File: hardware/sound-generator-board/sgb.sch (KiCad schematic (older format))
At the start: 53 parts, among them K1 CONN_3, P1 CONN_5, P10 CONN_4, P11 CONN_4, P12 CONN_4, P13 CONN_4, P14 CONN_4, P2 CONN_5, P4 CONN_6, P5 CONN_4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

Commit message: Turns out my transistor inverter isn't needed. That's good
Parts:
- removed P4: CONN_6, symbol CONN_6
- removed Q1: NPN, symbol NPN
- removed R4, R5: R, symbol R
- added K2: CONN_3, symbol CONN_3
- added unit 5 of U3
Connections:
- wire segments 340 -> 331

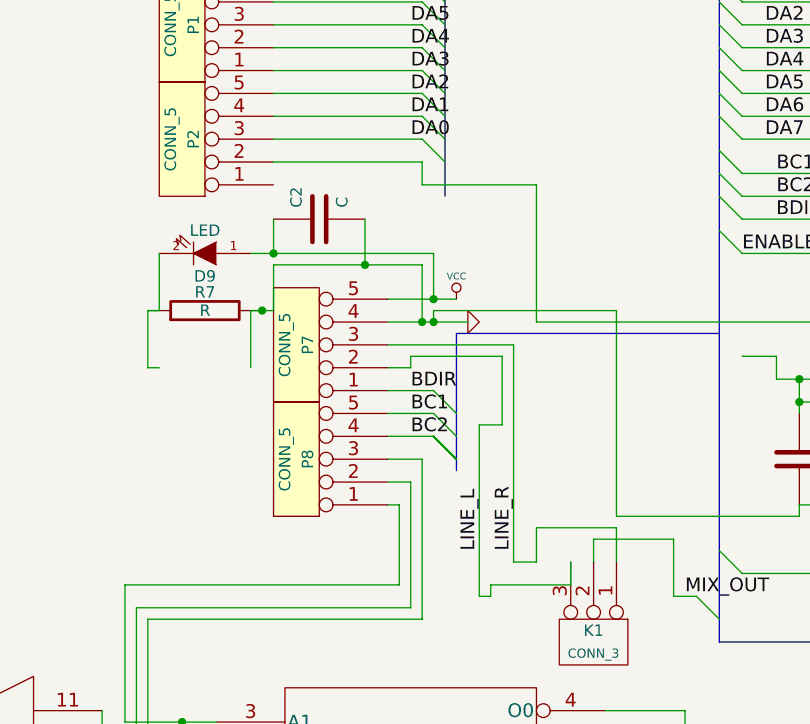
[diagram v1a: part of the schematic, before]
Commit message: Changed data bus pinout slightly to reduce noise on audio lines
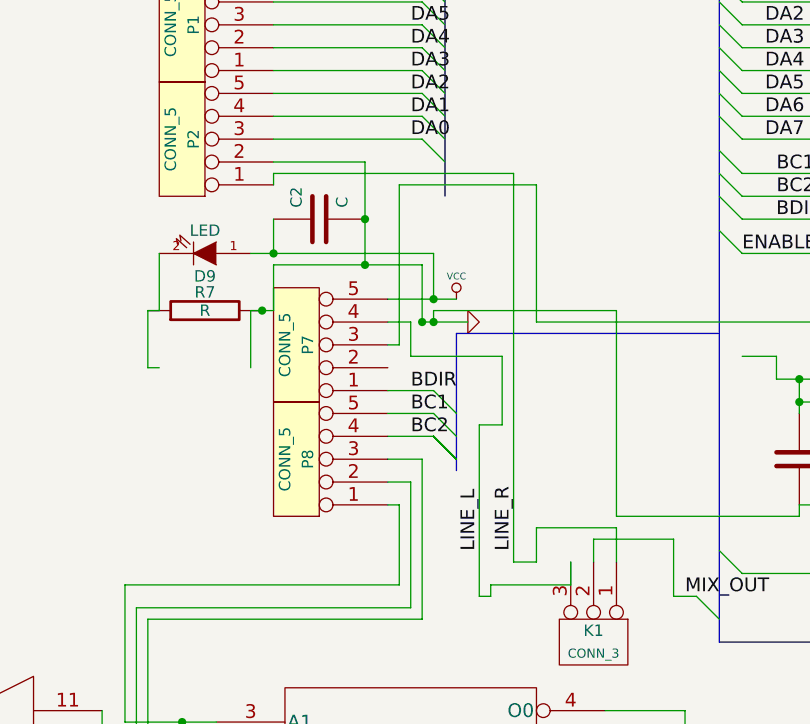
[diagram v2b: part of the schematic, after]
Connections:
- net CLOCK: now also P7.3; no longer P2.2
- net GND: now also P2.2; no longer P7.4
- net LINE_L: now also P7.4; no longer P7.2
- net LINE_R: now also P2.1; no longer P7.3
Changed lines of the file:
@@
-EESchema Schematic File Version 2  date Sat 03 Aug 2013 02:53:01 PM CEST
+EESchema Schematic File Version 2  date Sat 03 Aug 2013 07:12:06 PM CEST
 LIBS:power
 LIBS:device
@@
 $EndDescr
 Wire Wire Line
+	2350 3600 2350 3550
+Wire Wire Line
+	2350 3550 3400 3550
+Wire Wire Line
+	3400 3550 3400 5250
+Wire Wire Line
+	2850 4300 2900 4300
+Wire Wire Line
+	2900 4300 2900 3600
+Wire Wire Line
+	2900 3600 3500 3600
+Connection ~ 2750 3750
+Wire Wire Line
+	2350 3500 2750 3500
+Wire Wire Line
+	2750 3500 2750 3950
+Wire Wire Line
 	700  5900 700  6300
 Wire Wire Line
@@
 	8600 3600 8550 3600
 Connection ~ 2750 3950
-Wire Wire Line
-	2750 3750 2750 3950
 Wire Wire Line
 	8900 2600 8900 2550
@@
 	3350 4350 2950 4350
 Wire Wire Line
-	2950 4350 2950 4400
-Wire Wire Line
 	2850 5000 2900 5000
 Wire Wire Line
@@
 	2850 4600 3050 4600
 Wire Wire Line
-	2950 4400 2850 4400
-Wire Wire Line
-	2850 4200 3200 4200
-Wire Wire Line
 	2350 2700 3000 2700
 Wire Wire Line
@@
 Wire Wire Line
 	2350 3300 3000 3300
-Wire Wire Line
-	2350 3500 3000 3500
 Wire Wire Line
 	4800 3900 4400 3900
@@
 Connection ~ 3000 4200
 Wire Wire Line
-	3000 4200 3000 3950
+	3000 3950 3000 4200
 Wire Wire Line
 	3000 3950 2350 3950
@@
 	3500 4200 3500 3600
 Wire Wire Line
-	3500 3600 3000 3600
-Wire Wire Line
-	3000 3600 3000 3500
-Wire Wire Line
 	4400 3550 4800 3550
 Wire Wire Line
@@
 Wire Wire Line
 	4900 4450 4900 4050
-Wire Wire Line
-	2850 4300 3400 4300
-Wire Wire Line
-	3400 4300 3400 5250
 Wire Wire Line
 	3250 5400 3250 4650
@@
 Wire Wire Line
 	1600 6300 1600 5900
+Wire Wire Line
+	3000 4200 3200 4200
+Wire Wire Line
+	2950 4350 2950 4200
+Wire Wire Line
+	2950 4200 2850 4200
 $Comp
 L 74HC04 U3

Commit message: syncing
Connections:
- net CLOCK: now also P7.2; no longer P7.3
- net GND: now also P2.1, P7.3; no longer P2.2
- net LINE_R: now also P2.2; no longer P2.1
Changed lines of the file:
@@
-EESchema Schematic File Version 2  date Sat 03 Aug 2013 07:12:06 PM CEST
+EESchema Schematic File Version 2  date Sun 11 Aug 2013 02:48:30 PM CEST
 LIBS:power
 LIBS:device
@@
 $EndDescr
 Wire Wire Line
-	2350 3600 2350 3550
-Wire Wire Line
-	2350 3550 3400 3550
-Wire Wire Line
-	3400 3550 3400 5250
-Wire Wire Line
-	2850 4300 2900 4300
-Wire Wire Line
-	2900 4300 2900 3600
+	2350 3500 3400 3500
+Wire Wire Line
+	3400 3500 3400 5250
+Wire Wire Line
+	2850 4400 2900 4400
+Wire Wire Line
+	2900 4400 2900 3600
+Connection ~ 2450 3950
+Wire Wire Line
+	2350 3600 2450 3600
+Wire Wire Line
+	2450 3600 2450 3950
 Wire Wire Line
 	2900 3600 3500 3600
 Connection ~ 2750 3750
-Wire Wire Line
-	2350 3500 2750 3500
-Wire Wire Line
-	2750 3500 2750 3950
 Wire Wire Line
 	700  5900 700  6300
@@
 Connection ~ 3050 4200
 Wire Wire Line
-	3050 4200 3050 4150
-Wire Wire Line
-	3050 4150 3850 4150
+	3850 4150 3050 4150
 Wire Wire Line
 	3850 4150 3850 5050
@@
 Wire Wire Line
 	2950 4200 2850 4200
+Wire Wire Line
+	2850 4300 3050 4300
+Wire Wire Line
+	3050 4300 3050 4150
+Wire Wire Line
+	2750 3750 2750 3950
 $Comp
 L 74HC04 U3

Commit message: blolol
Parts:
- removed C5: C, symbol C
- removed D1, D2: DIODE, symbol DIODE
- removed R18: 8.2kΩ, symbol R
- removed R19: 10kΩ, symbol R
- added C10: 10µ, symbol CP1
- added C5: 47µ, symbol CP1
- added C9: 100µ, symbol CP1
- added P3: CONN_4, symbol CONN_4
- added Q1, Q3: BC547, TO92, symbol BC547
- added R4: 10k, symbol R
- added R5: 3k3, symbol R
- Q2: value BC182 -> BC547
- R16: value 10kΩ -> 1k5
- R17: value 680Ω -> 330R
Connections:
- net GND: now also C5.2, P3.2 (P2), P3.3 (P3), Q1.3 (E)
- net MIX_IN: no longer R1.2, R2.2, RV1.2
- net MIX_LINE_IN: now also C9.1; no longer Q2.3 (E), R17.2
- net MIX_OUT: now also C10.1
- net VCC: now also P3.1 (P1); no longer R16.1
- net at Q2.1 (C): now also C10.2, R5.2
- new net: R1.2, R2.2, RV1.2
- new net: C5.1, Q2.2 (B), R16.1, R4.2
- new net: C9.2, Q2.3 (E), Q3.1 (C)
- new net: Q1.1 (C), Q3.2 (B), R16.2
- new net: Q1.2 (B), Q3.3 (E), R17.2
- new net +12V: C4.1, P3.4 (P4), R4.1, R5.1
- no-connect marks 0 -> 6
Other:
- moved on the sheet: C4, Q2
